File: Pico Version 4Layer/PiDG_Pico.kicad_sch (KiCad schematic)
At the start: 43 parts, among them J1 Conn_02x05_Odd_Even, J10 Trig, J11 Laser Enable, J12 Pixel Reset, J14 Pico Socket A, J15 Pico Socket B, J16 Laser En/PWM Trig/GND, J2 Conn_02x05_Odd_Even, J3 Conn_02x05_Odd_Even, J4 Conn_02x05_Odd_Even, J5 Conn_02x05_Odd_Even, J6 Conn_02x05_Odd_Even, J7 Laser 1, J8 Laser 2, U1 74LVC1G04, U10 74LVC1G08, U11 Raspberry Pi Pico 2 W, U12 74LVC1G08, U13 UCC27524, U2 SN74LVC04AD, U3 74LVC1G04, U4 SN74LVC04AD, U5 74LVC1G04, U6 SN74LVC04AD, U7 74LVC1G08, U8 74LVC1G08

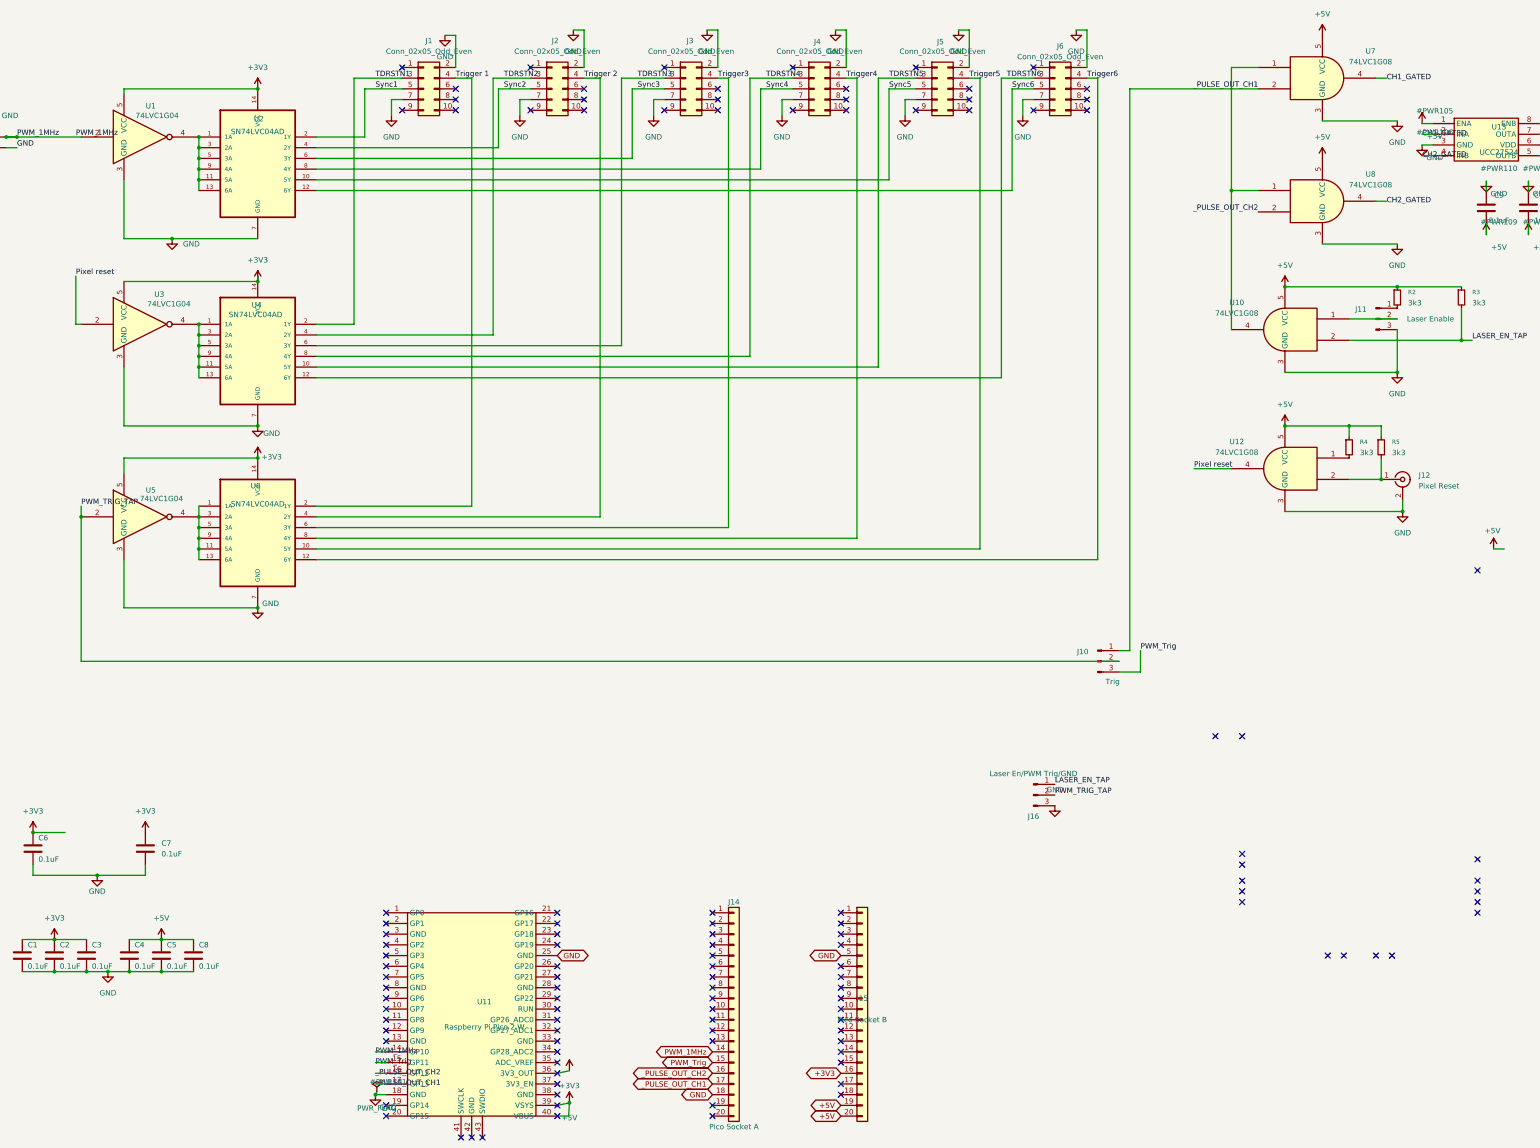
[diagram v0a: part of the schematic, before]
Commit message: Fix J15 socket pin mapping, bond all Pico grounds, clean net names
The J15 socket row was wired assuming pad m = Pico pin 20+m. The Pico
numbers like a DIP (down pins 1-20, back up 21-40), so pin 40 faces pin
1 and the correct relation is pad m = pin 41-m. J14 was already correct,
which fixed the geometry unambiguously.

As wired, inserting a module would have shorted its own 3V3_OUT to the
ground plane (J15.5), driven 5V into GP16/GP17 (J15.19/20), left the
logic bank U1-U6 unpowered (J15.16), and left the +5V rail with no
source at all (VBUS/VSYS unconnected). Neither ERC nor DRC can see this:
the symbol is self-consistent and U11 has no board footprint by design.

- J15 remapped: +5V -> pads 1/2 (VBUS/VSYS), +3V3 -> pad 5 (3V3_OUT),
  GPIO pads cleared. +3V3 entry rerouted by extending the existing
  x=180.5 vertical north to pad 5.
- All 8 module grounds bonded (J14 + J15 pads 3/8/13/18), up from one
  valid bond; the Teensy original grounded its MCU at 7 pins. Pads sit
  on the In1 ground plane, so the zone fill carries them.
- PiDG_Local:Raspberry_Pi_Pico pins 23/24/25 corrected to GND/GP18/GP19
  (were shifted one), pin 33 renamed AGND. Fixed in both the .kicad_sym
  and the lib_symbols copy cached in the schematic. Syncing the stale
  Description text also clears the long-standing "doesn't match copy in
  library" ERC warning.
- Resolved 23 no-connect conflicts, including 3 pre-existing ones on
  U11 pins 36/39/40.
- Firmware pin constants corrected to match the board: kPinCh1=13,
  kPinCh2=12, kPinMarker=11, kPinSync=10 (were GP2-GP5, which are
  no-connects here). As shipped the board would have appeared inert --
  both lasers and all six camera sync/trigger lines dead. Added a
  mapping table comment so the two cannot drift again.
- Net names reconciled with the schematic: 10 camera nets had decayed to
  Net-(Jn-PadN) placeholders. Named the 8 remaining anonymous nets
  (SYNC_N, TRIG_N, PIXRST_N, PIXRST_IN, PIXRST_GATE_EN, LASER_EN,
  LASER_EN_JMP, LASER_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
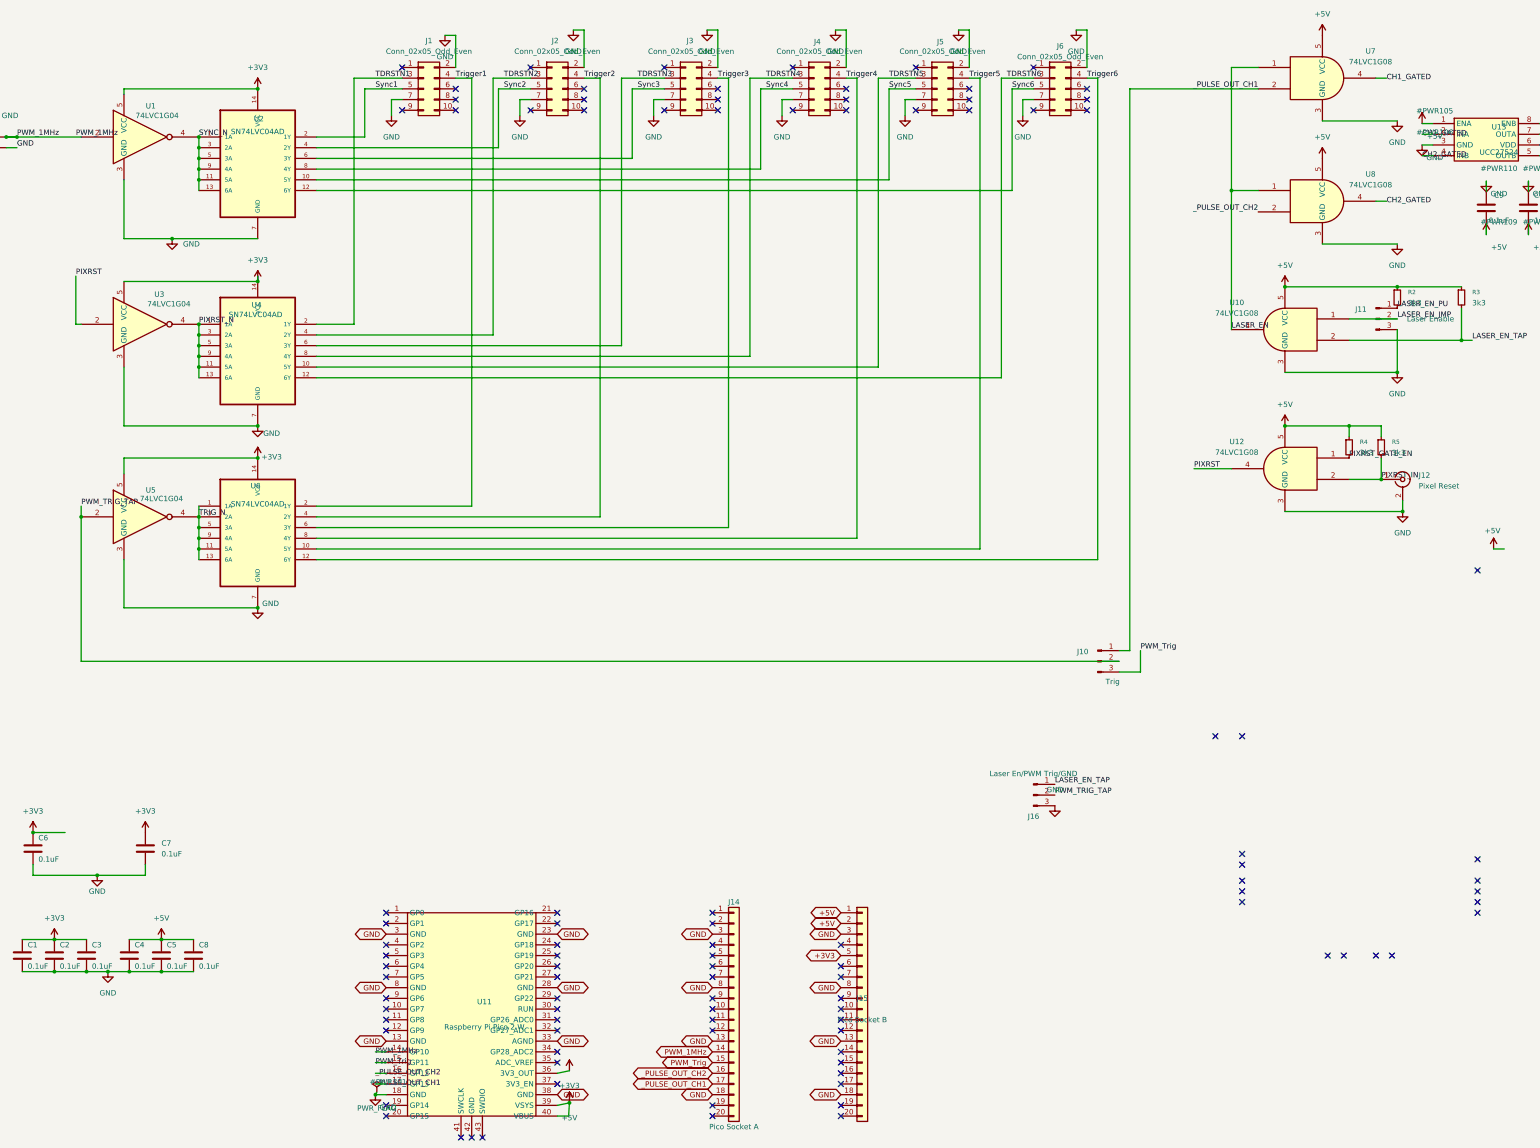
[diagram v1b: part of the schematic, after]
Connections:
- net +3V3: now also J15.5 (Pin_5); no longer J15.16 (Pin_16)
- net +5V: now also J15.1 (Pin_1), J15.2 (Pin_2); no longer J15.19 (Pin_19), J15.20 (Pin_20)
- net GND: now also J14.13 (Pin_13), J14.3 (Pin_3), J14.8 (Pin_8), J15.13 (Pin_13), J15.18 (Pin_18), J15.3 (Pin_3), J15.8 (Pin_8), U11.13 (GND), U11.23 (GND), U11.28 (GND), U11.3 (GND), U11.33 (AGND), U11.38 (GND), U11.8 (GND); no longer J15.5 (Pin_5), U11.25 (GND)
- net PIXRST_GATE_EN: now reaches R4.2, U12.1
- net LASER_EN: now reaches U10.4, U7.1, U8.1
- net PIXRST_IN: now reaches J12.1 (In), R5.2, U12.2
- net SYNC_N: now reaches U1.4, U2.1 (1A), U2.11 (5A), U2.13 (6A), U2.3 (2A), U2.5 (3A), U2.9 (4A)
- net LASER_EN_JMP: now reaches J11.2 (Pin_2), U10.1
- net PIXRST_N: now reaches U3.4, U4.1 (1A), U4.11 (5A), U4.13 (6A), U4.3 (2A), U4.5 (3A), U4.9 (4A)
- net TRIG_N: now reaches U5.4, U6.1 (1A), U6.11 (5A), U6.13 (6A), U6.3 (2A), U6.5 (3A), U6.9 (4A)
- net LASER_EN_PU: now reaches J11.1 (Pin_1), R2.2
- net Pixel reset renamed PIXRST
- net Trigger 1 renamed Trigger1
- net Trigger 2 renamed Trigger2
- no-connect marks 115 -> 100

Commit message: Add interlock pull-down and CH2 probe point; clear all DRC/ERC warnings
Board now reports 0 DRC violations and 0 ERC violations, with no warnings
of any kind. Board and schematic pad->net maps reconcile exactly (213
pads, 0 mismatches) and connectivity is bit-identical through the whole
cleanup, verified by diffing pad->net maps before and after.

Two parts added:

- R8 (10k, 0805) pulls LASER_EN_JMP / U10 pin 1 down, so the laser
  interlock now fails safe. Previously that node floated whenever no
  jumper was fitted on J11 and could drift high, arming both lasers. With
  the J11 1-2 jumper fitted R2's 3k3 pull-up still wins at ~3.76 V,
  comfortably above the 74LVC1G08's 2.0 V VIH at VCC=5 V. This hazard was
  inherited from the Teensy design, not introduced by the port.
- TP4 (1x02 vertical, CH2 + GND) gives _PULSE_OUT_CH2 a probe point. CH1
  has had one at J10.1 all along, but CH2 lost its only tap when the
  Teensy's J16/J17 breakouts disappeared into the sockets -- an awkward
  asymmetry for an instrument built around a CH1-CH2 delay. Routed as an
  18 mm B.Cu stub through the clear corridor at y=104, since J10's pad row
  at y=101 blocks the direct path east. ~0.24 ns round trip against a
  1-2 ns edge, so no ringing.

Warning cleanup (DRC 13 -> 0, ERC 68 -> 0):

- Clipped silkscreen that ran off the board edge on J16 and TP3, and moved
  TP4's reference text off J10's pad. Since trimming silk makes a
  footprint differ from its stock library, the trimmed outlines are now
  project-local *_EdgeTrim variants in libs/PiDG_Local.pretty, registered
  in fp-lib-table. Same part, same pads -- silkscreen only.
- Snapped the UCC27524 laser-driver block onto KiCad's 1.27 mm grid. It
  had been placed on a decimal-mm grid, which put 18 pins and 25 wire
  endpoints off-grid. Moved 18 symbols with wire preservation, then
  snapped the remaining loose wire endpoints.
- Removed 17 dangling no-connect flags and two orphan wires left over from
  the deleted U9 1.8 V LDO. Re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
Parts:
- added R8: 10k, Resistor_SMD:R_0805_2012Metric_Pad1.20x1.40mm_HandSolder, symbol Device:R_Small
- added TP4: CH2 monitor + GND, Connector_PinHeader_2.54mm:PinHeader_1x02_P2.54mm_Vertical, symbol Connector:Conn_01x02_Pin
- J16: footprint Connector_PinHeader_2.54mm:PinHeader_1x03_P2.54mm_Horizontal -> PiDG_Local:PinHeader_1x03_P2.54mm_Horizontal_EdgeTrim
- TP3: footprint Connector_PinHeader_2.54mm:PinHeader_1x02_P2.54mm_Horizontal -> PiDG_Local:PinHeader_1x02_P2.54mm_Horizontal_EdgeTrim
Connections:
- net GND: now also R8.2, TP4.2 (Pin_2)
- net LASER_EN_JMP: now also R8.1
- net _PULSE_OUT_CH2: now also TP4.1 (Pin_1)
- no-connect marks 100 -> 83
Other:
- moved on the sheet: C10, C9, R6, R7, U13

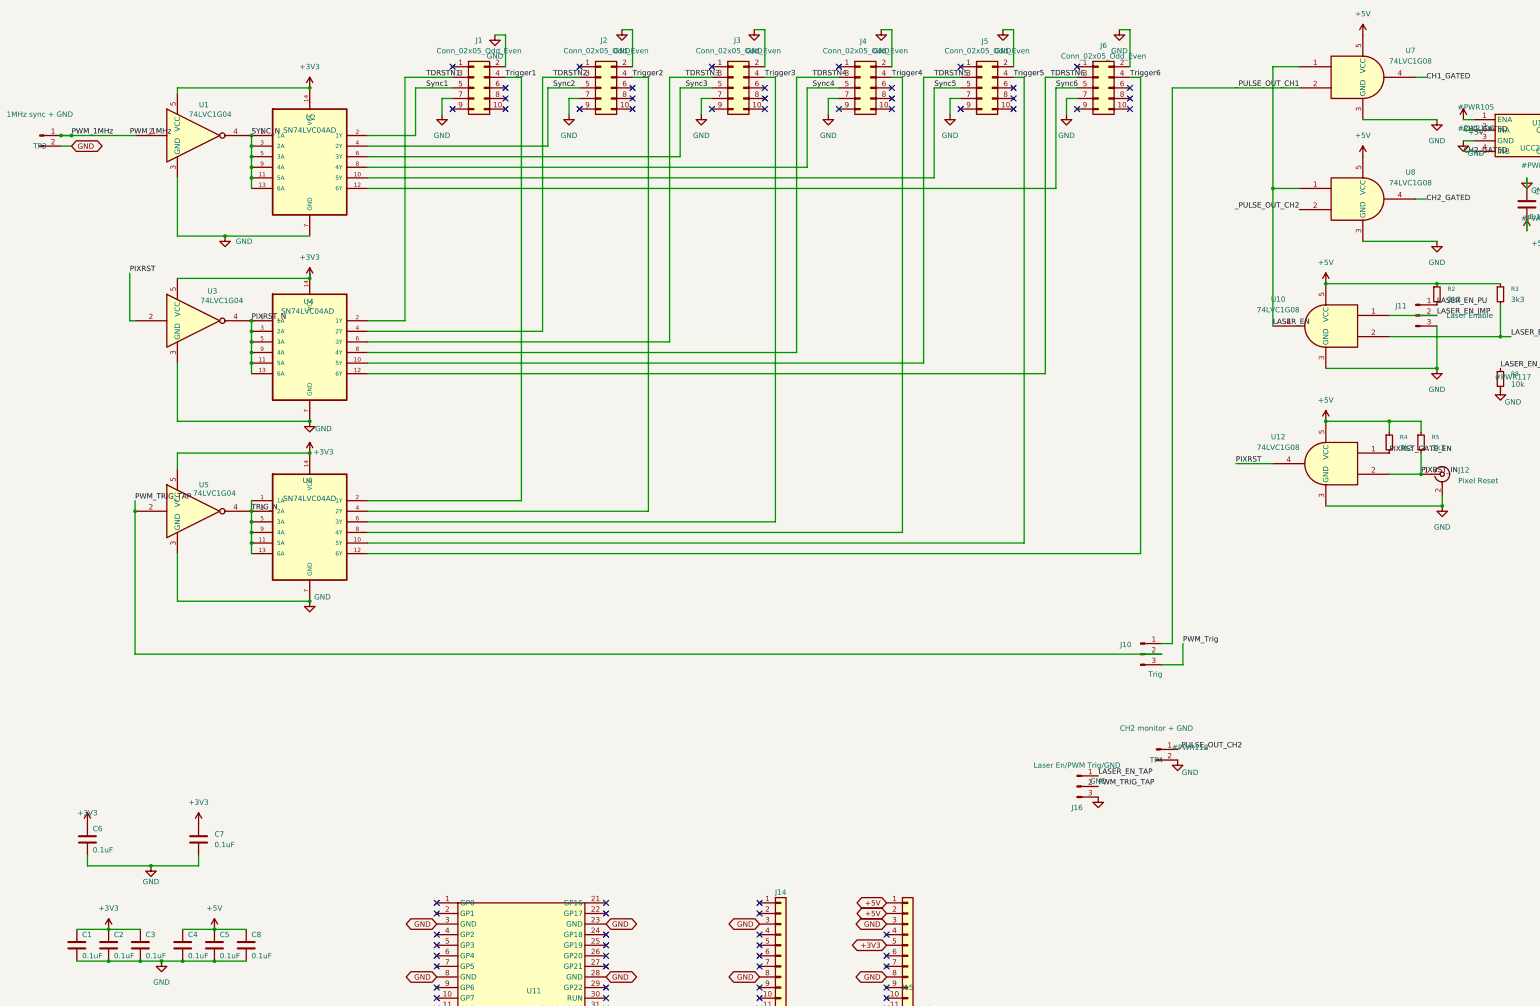
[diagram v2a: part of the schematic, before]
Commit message: Restore 1.8 V camera I/O rail; rebuild pixel-reset input as a 3.3 V Schmitt
The IDS UE-39B0XCP-E datasheet (part 1011378, rev 2026-01-09) documents
its I/O connector pins 3/4/5 -- TDRSTN, Trigger input, SYNC -- as
"(sensor), 1.8 V". The Teensy design's 1.8 V rail was therefore the
camera signalling rail, not vestigial. The Pico redesign had deleted it
and run the camera bank at 3.3 V, which would have driven 3.3 V into
1.8 V sensor pins on all 18 lines of six cameras. The harness does no
level translation, so the board itself must present 1.8 V.

Camera rail:
- Restore U9 = NCP718xSN180 (fixed 1.8 V LDO) at the Teensy's exact
  site. Feed it from +5 V rather than +3V3: NCP718 accepts 2.5-24 V, and
  +5 V is the In2 plane, reachable with one via.
- U1-U6 back on +1V8 via the five original camera-bank rail symbols.
  No part changes: SN74LVC04A / 74LVC1G04 inputs are 5.5 V tolerant
  independent of VCC, so at 1.8 V the bank itself translates down from
  the Pico's 3.3 V. At 1.8 V the drivers' 60-113 ohm output impedance
  also series-matches the ribbon, so no series resistors are needed.
- C6 -> 1 uF input cap, C7 -> 2.2 uF output cap. The Teensy's 1.8 V rail
  had only 4 x 0.1 uF, below NCP718's documented >= 1 uF stability floor.
- Board: the redesign had deleted U9 and bridged its OUT pad straight to
  the IN side with one segment, merging the two rails. Deleting that
  bridge and re-netting restores the Teensy's original +1V8 output route
  unchanged. U9's GND pad gets a via under the body to the In1 plane.

Pixel-reset input:
- U12 74LVC1G08 @ +5 V -> 74LVC1G17 Schmitt buffer @ +3V3 (drop-in on
  the SOT-23-5 pads). At VCC = 5 V an LVC input needs 0.7 x VCC = 3.5 V
  to read high, so a 3.3 V source could not reliably release reset, and
  a bare BNC input had no hysteresis. At 3.3 V the 1G17 switches low
  below 0.89 V and high above ~1.92-2.1 V with 0.5-0.8 V hysteresis, and
  tolerates 5.5 V input: 3.3 V / 5 V CMOS, TTL and open-drain sources
  all work. A 1.8 V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
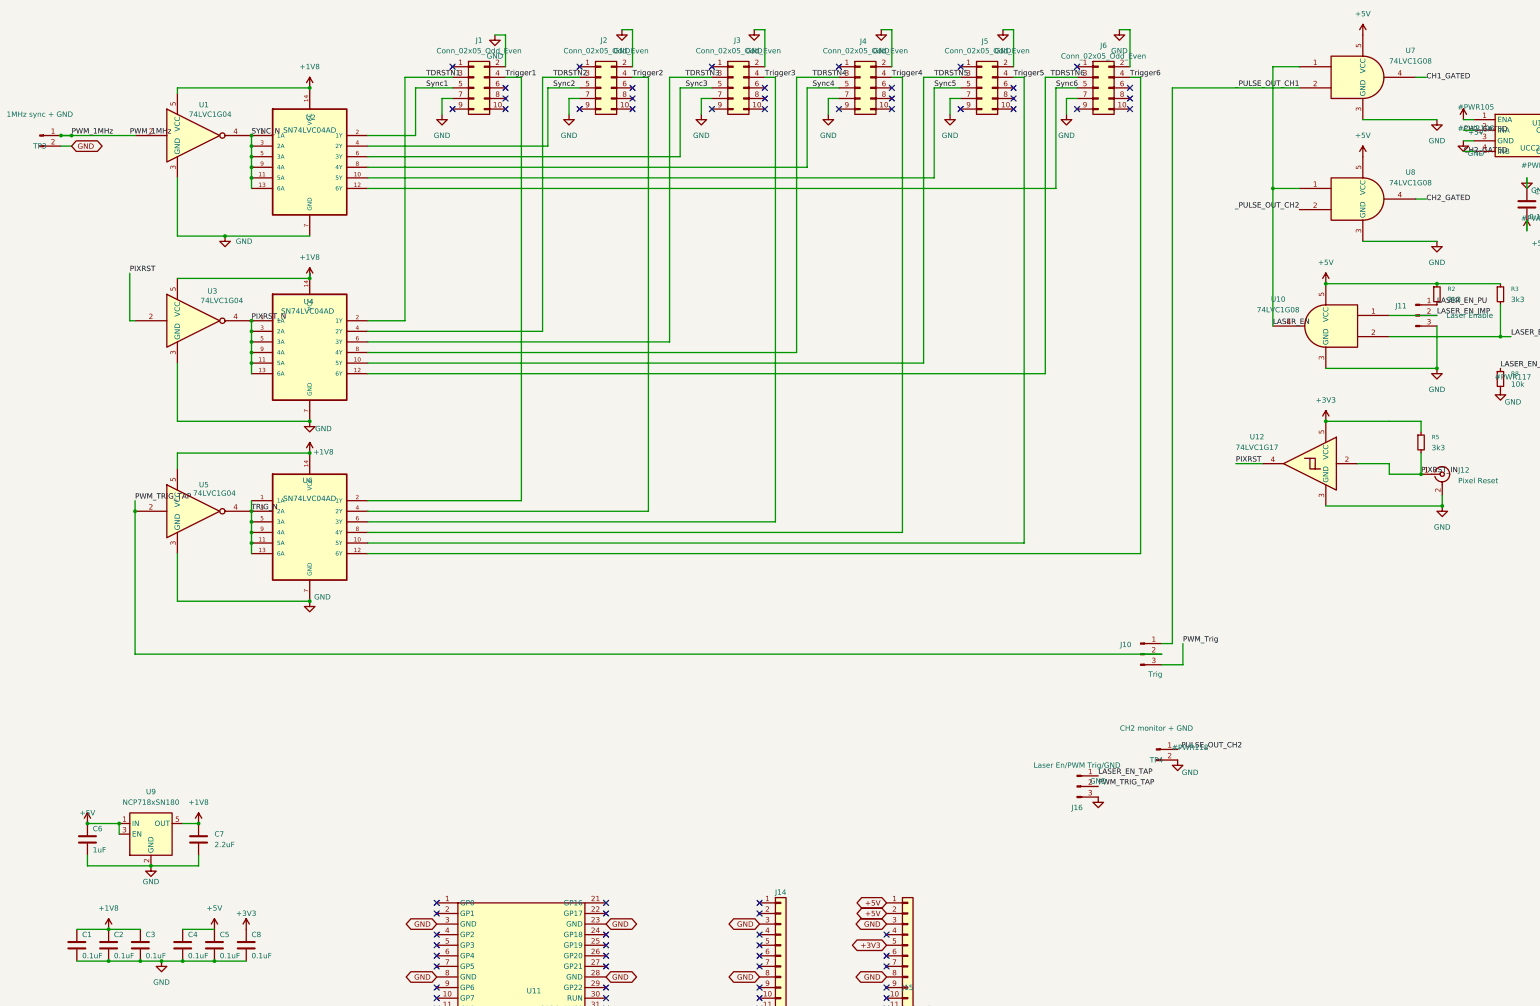
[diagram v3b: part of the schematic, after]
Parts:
- removed R4: 3k3, Resistor_SMD:R_0805_2012Metric_Pad1.20x1.40mm_HandSolder, symbol Device:R_Small
- added U9: NCP718xSN180, Package_TO_SOT_SMD:SOT-23-5_HandSoldering, symbol Regulator_Linear:NCP718xSN180
- C6: value 0.1uF -> 1uF
- C7: value 0.1uF -> 2.2uF
- U12: value 74LVC1G08 -> 74LVC1G17; symbol 74xGxx:74LVC1G08 -> 74xGxx:74LVC1G17
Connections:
- net +3V3: now also C8.1, R5.1, U12.5 (VCC); no longer C1.1, C2.1, C3.1, C6.1, C7.1, U1.5 (VCC), U2.14 (VCC), U3.5 (VCC), U4.14 (VCC), U5.5 (VCC), U6.14 (VCC)
- net +5V: now also C6.1, U9.1 (IN), U9.3 (EN); no longer C8.1, R5.1, U12.5 (VCC)
- net GND: now also U9.2 (GND)
- net PIXRST_GATE_EN: no longer names the net of U12.1 (NC)
- new net +1V8: C1.1, C2.1, C3.1, C7.1, U1.5 (VCC), U2.14 (VCC), U3.5 (VCC), U4.14 (VCC), U5.5 (VCC), U6.14 (VCC), U9.5 (OUT)
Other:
- moved on the sheet: U12
